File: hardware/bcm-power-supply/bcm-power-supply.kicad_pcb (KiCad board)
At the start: 2 copper layers, 82.8 x 70.1 mm, 25 parts, among them J1 Screw_Terminal_01x02, J2 Conn_02x08_Odd_Even, J3 Conn_02x08_Odd_Even, J4 Conn_01x04, J5 Conn_01x04, U1 N7812, U2 N7812

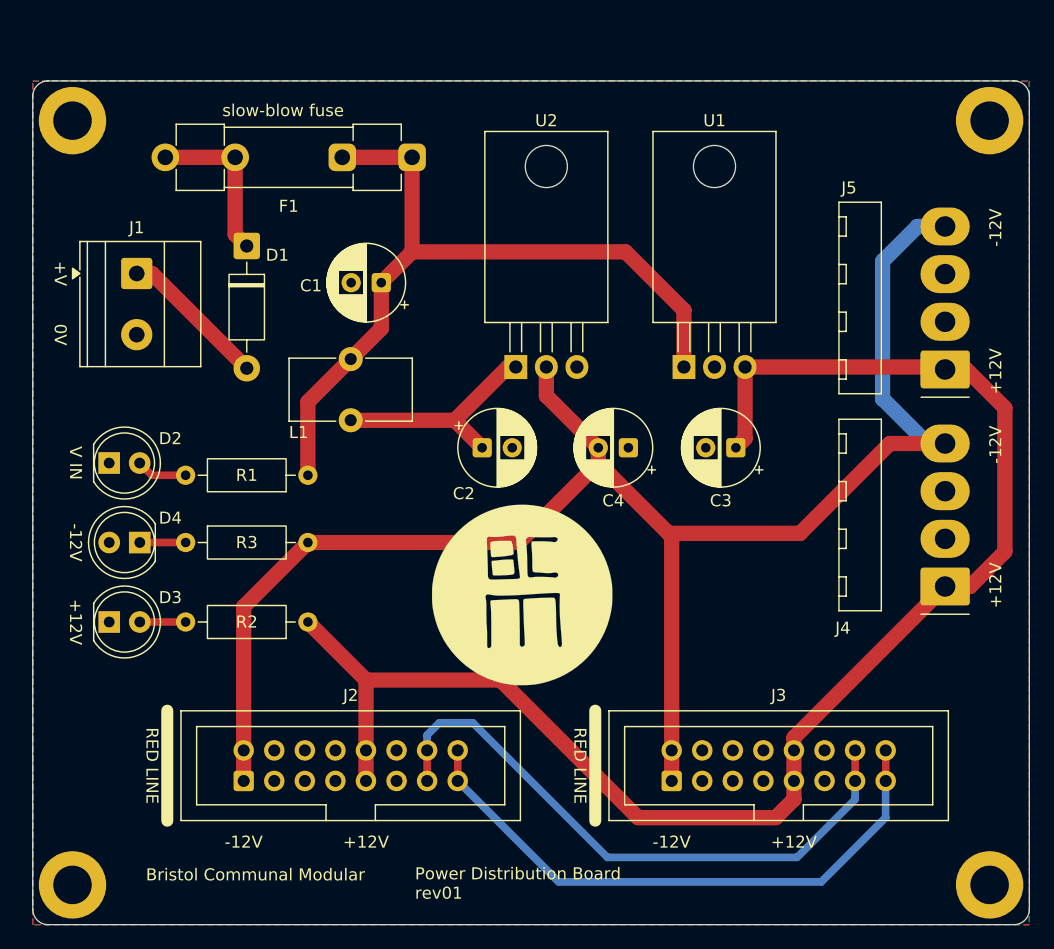
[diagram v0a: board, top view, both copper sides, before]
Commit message: Updating with 5v output
And making the board smaller
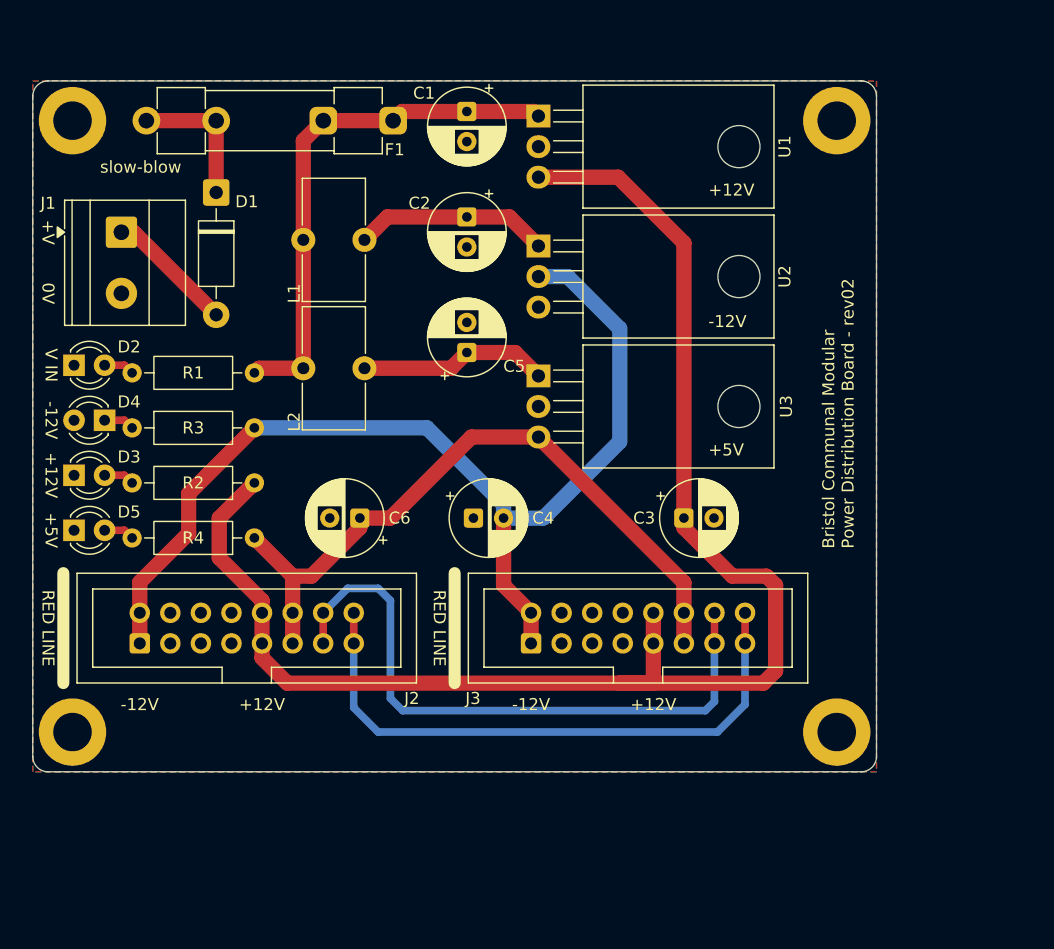
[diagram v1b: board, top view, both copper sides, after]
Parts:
- removed J4, J5: Conn_01x04, Connector_Molex:Molex_KK-396_A-41792-0004_1x04_P3.96mm_Horizontal
- removed Ref**: Val**, BCM_Graphics:BCM_Logo_small_15mmx15mm
- added C5: 10uF, Capacitor_THT:CP_Radial_D6.3mm_P2.50mm, F.Cu at (96.3, 82.8)
- added C6: 22uF, Capacitor_THT:CP_Radial_D6.3mm_P2.50mm, F.Cu at (87.4, 96.5)
- added D5: LED, LED_THT:LED_D3.0mm, F.Cu at (63.6, 97.5)
- added L2: 10uH, Inductor_THT:L_Toroid_Vertical_L10.0mm_W5.0mm_P5.08mm, F.Cu at (82.7, 84.1)
- added R4: 4k7, Resistor_THT:R_Axial_DIN0207_L6.3mm_D2.5mm_P10.16mm_Horizontal, F.Cu at (78.6, 98.2)
- added U3: N7805, Package_TO_SOT_THT:TO-220-3_Horizontal_TabDown, F.Cu at (102.2, 84.7)
- D2, D3, D4: footprint LED_THT:LED_D5.0mm -> LED_THT:LED_D3.0mm
- moved U1 24.1 mm to (102.2, 63.1), turned to -90 degrees
- moved C2 19.2 mm to (96.3, 71.5), turned to -90 degrees
- moved H4 18.0 mm to (127.0, 114.3)
- moved J3 16.3 mm to (101.6, 106.9)
- moved C1 15.9 mm to (96.3, 62.7), turned to -90 degrees
- moved J2 14.3 mm to (69.1, 106.9)
- moved C4 14.1 mm to (96.8, 96.5), turned to 0 degrees
- moved H2 12.7 mm to (63.5, 114.3)
- moved H3 12.7 mm to (127.0, 63.5)
- moved D3 12.5 mm to (63.6, 93.0)
- moved R2 12.4 mm to (78.6, 93.6)
- moved L1 10.7 mm to (82.7, 73.4), turned to 90 degrees
- moved D4 10.6 mm to (66.2, 88.4)
- moved R3 10.5 mm to (68.5, 89.0)
- moved U2 10.2 mm to (102.2, 73.9), turned to -90 degrees
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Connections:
- net /power_filtered renamed /power_neg12_filtered
- J2 pad 11: unconnected-(J2A-+5V-Pad11)_1 -> +5V
- J2 pad 12: unconnected-(J2A-+5V-Pad11) -> +5V
- J3 pad 11: unconnected-(J3A-+5V-Pad11)_1 -> +5V
- J3 pad 12: unconnected-(J3A-+5V-Pad11) -> +5V
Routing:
- net +5V: track 0.00 -> 57.9 mm
- net -12V: track 138.2 -> 87.9 mm
- net VCC: track 65.1 -> 43.8 mm
- net /power_5_filtered: track 0.00 -> 15.8 mm
- net +12V: track 127.1 -> 124.5 mm
- net Net-(D5-A): track 0.00 -> 2.55 mm
- net /power_neg12_filtered: track 18.8 -> 16.2 mm
- net /eurorack_cv_bus: track 50.5 -> 52.5 mm
- net /power_in_diode: track 13.6 -> 11.8 mm
- net /power_in_raw: track 12.4 -> 10.7 mm
- net Net-(D2-A): track 4.24 -> 2.55 mm
- net Net-(D4-K): track 3.81 -> 2.55 mm
- net Net-(D3-A): track 3.81 -> 2.55 mm
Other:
- board size 82.8 x 70.1 mm -> 70.1 x 57.4 mm
- board text added: "${COMPANY} ${TITLE} - ${REVISION}"
- board text added: "+5V"
- board text added: "slow-blow"
- board text removed: "${COMPANY}"
- board text removed: "${TITLE} ${REVISION}"
- board text removed: "slow-blow fuse"

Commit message: Updating power supply board to give more space for regulators
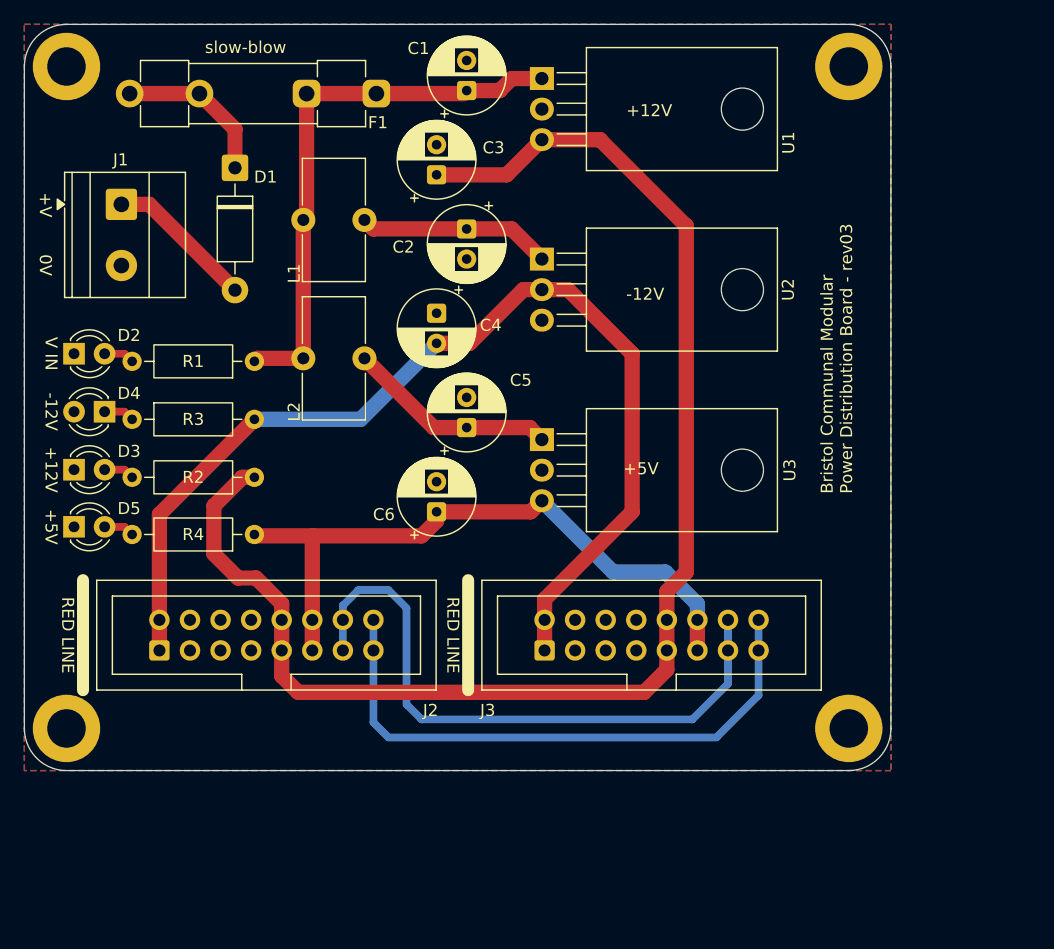
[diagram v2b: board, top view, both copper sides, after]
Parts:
- added Ref**: Val**, BCM_Graphics:BCM_Logo_small_15mmx15mm, B.Cu at (110.8, 85.2)
- moved C3 35.2 mm to (93.8, 68.0), turned to 90 degrees
- moved C4 17.3 mm to (93.8, 79.5), turned to -90 degrees
- moved C6 6.40 mm to (93.8, 96.0), turned to 90 degrees
- moved C5 6.24 mm to (96.2, 89.0)
- moved U3 5.30 mm to (102.5, 90.0)
- moved H3 4.61 mm to (128.0, 59.0)
- moved H1 4.53 mm to (63.0, 59.0)
- moved U1 3.13 mm to (102.5, 60.0)
- moved F1 2.64 mm to (88.8, 61.2)
- moved D1 2.58 mm to (77.0, 67.4)
- moved J1 2.32 mm to (67.6, 70.5)
- moved C1 1.74 mm to (96.2, 61.0), turned to 90 degrees
- moved J2 1.74 mm to (70.7, 107.5)
- moved L1 1.66 mm to (82.7, 71.8)
- moved J3 1.27 mm to (102.7, 107.5)
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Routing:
- net +12V: track 124.5 -> 117.7 mm
- net VCC: track 43.8 -> 46.3 mm
- net +5V: track 57.9 -> 55.5 mm
- net /power_5_filtered: track 15.8 -> 17.5 mm
- net /power_in_raw: track 10.7 -> 12.4 mm
- net /power_in_diode: track 11.8 -> 13.2 mm
- net /eurorack_gate_bus: track 49.8 -> 48.8 mm
- net /eurorack_cv_bus: track 52.5 -> 51.9 mm
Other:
- board size 70.1 x 57.4 mm -> 72 x 62 mm
